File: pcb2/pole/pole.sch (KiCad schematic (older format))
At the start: 21 parts, among them IC1 LMx93, IC2 STM32F0xxKxTx, P1 POWER_IN, P2 BUS_IN, P3 BUS_OUT, P4 SWD_TC, P5 LEDs, Q1 MTM232270LBF, Q2 MTM232270LBF, Q3 MTM232270LBF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

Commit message: Initial layout of f030
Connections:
- net BUS: now also IC2.19 (PA9)
- net NRST: now also C5.2, IC2.4 (NRST)
- net SWDCLK: now also IC2.24 (PA14)
- net SWDIO: now also IC2.23 (PA13)
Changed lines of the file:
@@
 $EndComp
 $Comp
-L GND #PWR5
+L GND #PWR01
 U 1 1 56F1CE8F
 P 3450 3000
-F 0 "#PWR5" H 3450 2750 50  0001 C CNN
+F 0 "#PWR01" H 3450 2750 50  0001 C CNN
 F 1 "GND" H 3450 2850 50  0000 C CNN
 F 2 "" H 3450 3000 50  0000 C CNN
@@
 	3450 2900 3450 3000
 $Comp
-L +12V #PWR4
+L +12V #PWR02
 U 1 1 56F1CF45
 P 3450 2700
-F 0 "#PWR4" H 3450 2550 50  0001 C CNN
+F 0 "#PWR02" H 3450 2550 50  0001 C CNN
 F 1 "+12V" H 3450 2840 50  0000 C CNN
 F 2 "" H 3450 2700 50  0000 C CNN
@@
 	3450 2800 3450 2700
 $Comp
-L PWR_FLAG #FLG1
+L PWR_FLAG #FLG03
 U 1 1 56F1CF7B
 P 3300 2800
-F 0 "#FLG1" H 3300 2895 50  0001 C CNN
+F 0 "#FLG03" H 3300 2895 50  0001 C CNN
 F 1 "PWR_FLAG" H 3300 2980 50  0001 C CNN
 F 2 "" H 3300 2800 50  0000 C CNN
@@
 Connection ~ 3300 2900
 $Comp
-L PWR_FLAG #FLG2
+L PWR_FLAG #FLG04
 U 1 1 56F1CFB0
 P 3300 2900
-F 0 "#FLG2" H 3300 2995 50  0001 C CNN
+F 0 "#FLG04" H 3300 2995 50  0001 C CNN
 F 1 "PWR_FLAG" H 3300 3080 50  0001 C CNN
 F 2 "" H 3300 2900 50  0000 C CNN
@@
 BUS_B
 $Comp
-L GND #PWR3
+L GND #PWR05
 U 1 1 56F1D45F
 P 3150 6050
-F 0 "#PWR3" H 3150 5800 50  0001 C CNN
+F 0 "#PWR05" H 3150 5800 50  0001 C CNN
 F 1 "GND" H 3150 5900 50  0000 C CNN
 F 2 "" H 3150 6050 50  0000 C CNN
@@
 BUS
 $Comp
-L +3V3 #PWR1
+L +3V3 #PWR06
 U 1 1 56F1D52A
 P 3150 5200
-F 0 "#PWR1" H 3150 5050 50  0001 C CNN
+F 0 "#PWR06" H 3150 5050 50  0001 C CNN
 F 1 "+3V3" H 3150 5340 50  0000 C CNN
 F 2 "" H 3150 5200 50  0000 C CNN
@@
 $EndComp
 $Comp
-L GND #PWR2
+L GND #PWR07
 U 1 1 56F1D54C
 P 3150 5400
-F 0 "#PWR2" H 3150 5150 50  0001 C CNN
+F 0 "#PWR07" H 3150 5150 50  0001 C CNN
 F 1 "GND" H 3150 5250 50  0001 C CNN
 F 2 "" H 3150 5400 50  0000 C CNN
@@
 NoConn ~ 7500 2450
 $Comp
-L GND #PWR20
+L GND #PWR08
 U 1 1 56F1D83D
 P 6700 2450
-F 0 "#PWR20" H 6700 2200 50  0001 C CNN
+F 0 "#PWR08" H 6700 2200 50  0001 C CNN
 F 1 "GND" H 6700 2300 50  0000 C CNN
 F 2 "" H 6700 2450 50  0000 C CNN
@@
 $EndComp
 $Comp
-L +3V3 #PWR19
+L +3V3 #PWR09
 U 1 1 56F1D861
 P 6700 2250
-F 0 "#PWR19" H 6700 2100 50  0001 C CNN
+F 0 "#PWR09" H 6700 2100 50  0001 C CNN
 F 1 "+3V3" H 6700 2390 50  0000 C CNN
 F 2 "" H 6700 2250 50  0000 C CNN
@@
 NRST
 $Comp
-L GND #PWR13
+L GND #PWR010
 U 1 1 56F1D8BE
 P 4850 3250
-F 0 "#PWR13" H 4850 3000 50  0001 C CNN
+F 0 "#PWR010" H 4850 3000 50  0001 C CNN
 F 1 "GND" H 4850 3100 50  0000 C CNN
 F 2 "" H 4850 3250 50  0000 C CNN
@@
 $EndComp
 Wire Wire Line
-	4850 3150 4700 3150
-$Comp
-L GND #PWR11
+	4300 3150 4850 3150
+$Comp
+L GND #PWR011
 U 1 1 56F1D93B
 P 4700 3350
-F 0 "#PWR11" H 4700 3100 50  0001 C CNN
+F 0 "#PWR011" H 4700 3100 50  0001 C CNN
 F 1 "GND" H 4700 3200 50  0000 C CNN
 F 2 "" H 4700 3350 50  0000 C CNN
@@
 $EndComp
 $Comp
-L GND #PWR12
+L GND #PWR012
 U 1 1 56F1D985
 P 4850 2950
-F 0 "#PWR12" H 4850 2700 50  0001 C CNN
+F 0 "#PWR012" H 4850 2700 50  0001 C CNN
 F 1 "GND" H 4850 2800 50  0001 C CNN
 F 2 "" H 4850 2950 50  0000 C CNN
@@
 $EndComp
 $Comp
-L +3V3 #PWR7
+L +3V3 #PWR013
 U 1 1 56F1DBBD
 P 4350 2650
-F 0 "#PWR7" H 4350 2500 50  0001 C CNN
+F 0 "#PWR013" H 4350 2500 50  0001 C CNN
 F 1 "+3V3" H 4350 2790 50  0000 C CNN
 F 2 "" H 4350 2650 50  0000 C CNN
@@
 	4500 2850 4350 2850
 $Comp
-L GND #PWR8
+L GND #PWR014
 U 1 1 56F1DC6A
 P 4350 2850
-F 0 "#PWR8" H 4350 2600 50  0001 C CNN
+F 0 "#PWR014" H 4350 2600 50  0001 C CNN
 F 1 "GND" H 4350 2700 50  0000 C CNN
 F 2 "" H 4350 2850 50  0000 C CNN
@@
 	4700 2750 4700 2550
 $Comp
-L +3V3 #PWR9
+L +3V3 #PWR015
 U 1 1 56F1DCD3
 P 4700 2550
-F 0 "#PWR9" H 4700 2400 50  0001 C CNN
+F 0 "#PWR015" H 4700 2400 50  0001 C CNN
 F 1 "+3V3" H 4700 2690 50  0000 C CNN
 F 2 "" H 4700 2550 50  0000 C CNN
@@
 $EndComp
 $Comp
-L GND #PWR10
+L GND #PWR016
 U 1 1 56F1DCFF
 P 4700 2950
-F 0 "#PWR10" H 4700 2700 50  0001 C CNN
+F 0 "#PWR016" H 4700 2700 50  0001 C CNN
 F 1 "GND" H 4700 2800 50  0000 C CNN
 F 2 "" H 4700 2950 50  0000 C CNN
@@
 Connection ~ 4700 2750
 $Comp
-L +12V #PWR26
+L +12V #PWR017
 U 1 1 56F1E092
 P 9600 4000
-F 0 "#PWR26" H 9600 3850 50  0001 C CNN
+F 0 "#PWR017" H 9600 3850 50  0001 C CNN
 F 1 "+12V" H 9600 4140 50  0000 C CNN
 F 2 "" H 9600 4000 50  0000 C CNN
@@
 DRIVE_R
 $Comp
-L GND #PWR21
+L GND #PWR018
 U 1 1 56F1E226
 P 7900 3650
-F 0 "#PWR21" H 7900 3400 50  0001 C CNN
+F 0 "#PWR018" H 7900 3400 50  0001 C CNN
 F 1 "GND" H 7900 3500 50  0000 C CNN
 F 2 "" H 7900 3650 50  0000 C CNN
@@
 DRIVE_G
 $Comp
-L GND #PWR22
+L GND #PWR019
 U 1 1 56F1E522
 P 7900 4400
-F 0 "#PWR22" H 7900 4150 50  0001 C CNN
+F 0 "#PWR019" H 7900 4150 50  0001 C CNN
 F 1 "GND" H 7900 4250 50  0000 C CNN
 F 2 "" H 7900 4400 50  0000 C CNN
@@
 DRIVE_B
 $Comp
-L GND #PWR23
+L GND #PWR020
 U 1 1 56F1E671
 P 7900 5150
-F 0 "#PWR23" H 7900 4900 50  0001 C CNN
+F 0 "#PWR020" H 7900 4900 50  0001 C CNN
 F 1 "GND" H 7900 5000 50  0000 C CNN
 F 2 "" H 7900 5150 50  0000 C CNN
@@
 Text Label 7600 4950 2    60   ~ 0
 LED_B
-Text Label 6150 3050 0    60   ~ 0
+Text Label 5650 3550 0    60   ~ 0
 BUS
 Text Label 6150 3150 0    60   ~ 0
@@
 PIEZO
 $Comp
-L GND #PWR25
+L GND #PWR021
 U 1 1 56F594BA
 P 9550 5800
-F 0 "#PWR25" H 9550 5550 50  0001 C CNN
+F 0 "#PWR021" H 9550 5550 50  0001 C CNN
 F 1 "GND" H 9550 5650 50  0000 C CNN
 F 2 "" H 9550 5800 50  0000 C CNN
@@
 $EndComp
 $Comp
-L +12V #PWR24
+L +12V #PWR022
 U 1 1 56F59754
 P 9550 5200
-F 0 "#PWR24" H 9550 5050 50  0001 C CNN
+F 0 "#PWR022" H 9550 5050 50  0001 C CNN
 F 1 "+12V" H 9550 5340 50  0000 C CNN
 F 2 "" H 9550 5200 50  0000 C CNN
@@
 Connection ~ 4100 5300
 $Comp
-L +3V3 #PWR6
+L +3V3 #PWR023
 U 1 1 56F59A49
 P 4100 5000
-F 0 "#PWR6" H 4100 4850 50  0001 C CNN
+F 0 "#PWR023" H 4100 4850 50  0001 C CNN
 F 1 "+3V3" H 4100 5140 50  0000 C CNN
 F 2 "" H 4100 5000 50  0000 C CNN
@@
 $EndComp
 $Comp
-L +12V #PWR14
+L +12V #PWR024
 U 1 1 56F59EBA
 P 5200 5350
-F 0 "#PWR14" H 5200 5200 50  0001 C CNN
+F 0 "#PWR024" H 5200 5200 50  0001 C CNN
 F 1 "+12V" H 5200 5490 50  0000 C CNN
 F 2 "" H 5200 5350 50  0000 C CNN
@@
 $EndComp
 $Comp
-L GND #PWR15
+L GND #PWR025
 U 1 1 56F59F39
 P 5200 5650
-F 0 "#PWR15" H 5200 5400 50  0001 C CNN
+F 0 "#PWR025" H 5200 5400 50  0001 C CNN
 F 1 "GND" H 5200 5500 50  0000 C CNN
 F 2 "" H 5200 5650 50  0000 C CNN
@@
 	5200 5350 5300 5350
 $Comp
-L +3V3 #PWR17
+L +3V3 #PWR026
 U 1 1 56F59FB2
 P 6200 5350
-F 0 "#PWR17" H 6200 5200 50  0001 C CNN
+F 0 "#PWR026" H 6200 5200 50  0001 C CNN
 F 1 "+3V3" H 6200 5490 50  0000 C CNN
 F 2 "" H 6200 5350 50  0000 C CNN
@@
 $EndComp
 $Comp
-L GND #PWR18
+L GND #PWR027
 U 1 1 56F5A070
 P 6200 5650
-F 0 "#PWR18" H 6200 5400 50  0001 C CNN
+F 0 "#PWR027" H 6200 5400 50  0001 C CNN
 F 1 "GND" H 6200 5500 50  0000 C CNN
 F 2 "" H 6200 5650 50  0000 C CNN
@@
 $EndComp
 $Comp
-L GND #PWR16
+L GND #PWR028
 U 1 1 56F5A0AE
 P 5700 5650
-F 0 "#PWR16" H 5700 5400 50  0001 C CNN
+F 0 "#PWR028" H 5700 5400 50  0001 C CNN
 F 1 "GND" H 5700 5500 50  0000 C CNN
 F 2 "" H 5700 5650 50  0000 C CNN
@@
 	1    0    0    -1
 $EndComp
+Text Label 4300 3150 2    60   ~ 0
+NRST
+Text Label 5650 3950 0    60   ~ 0
+SWDIO
+Text Label 5650 4050 0    60   ~ 0
+SWDCLK
+Connection ~ 4700 3150
 $EndSCHEMATC

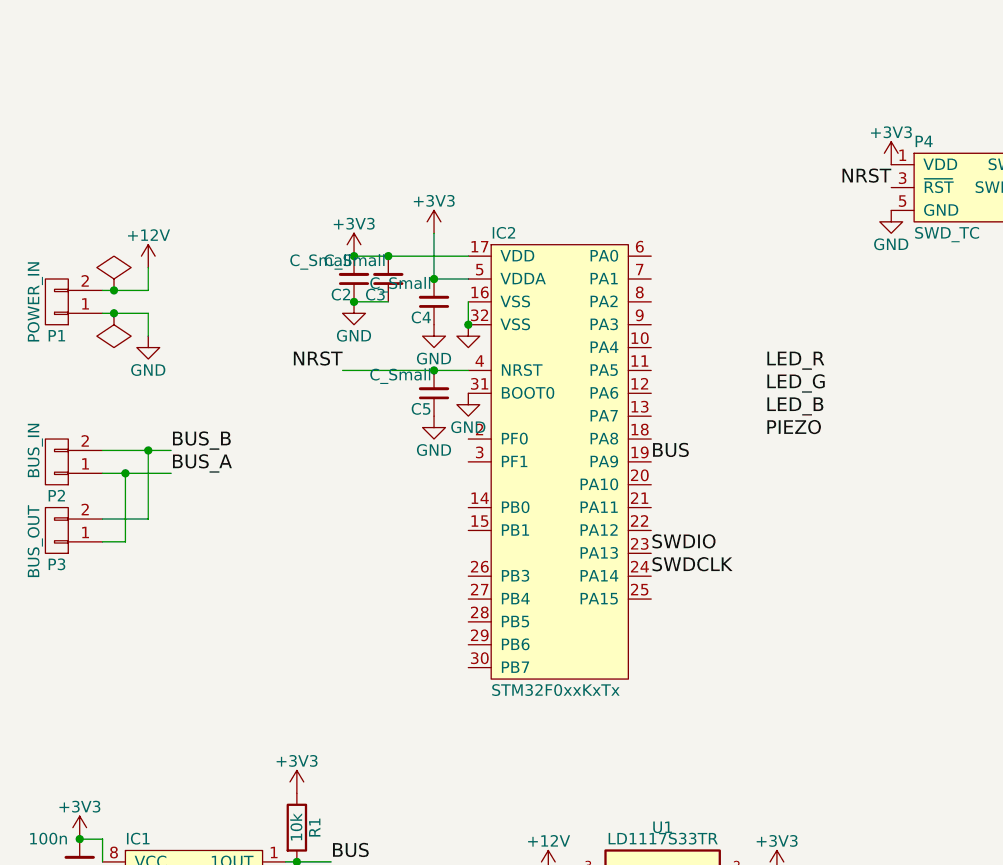
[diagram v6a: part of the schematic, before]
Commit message: Use STM32F051, changed FPs to agg-kicad
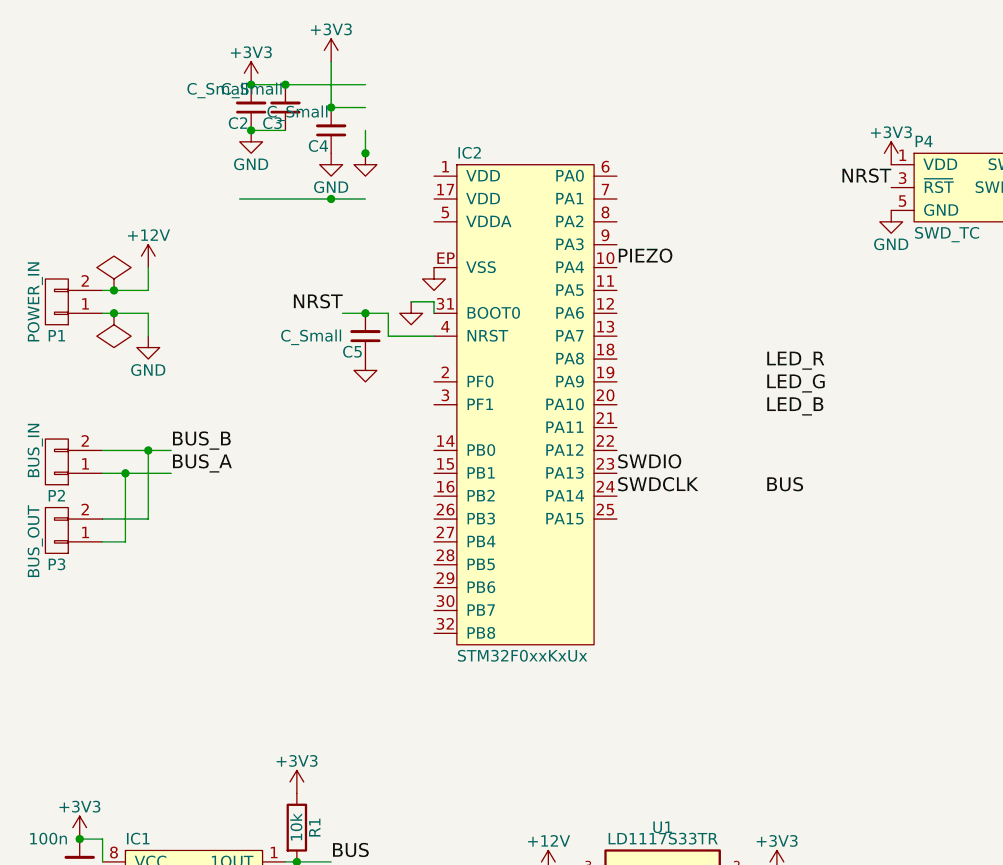
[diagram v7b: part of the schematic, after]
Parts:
- removed IC2: STM32F0xxKxTx, agg:LQFP-32, symbol STM32F0xxKxTx
- added IC2: STM32F0xxKxUx, agg:QFN-32-EP-ST, symbol STM32F0xxKxUx
- Q1, Q2, Q3, Q4: footprint thegrid:SOT-323 -> agg:SOT-323
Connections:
- wire segments 25 -> 30
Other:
- moved on the sheet: C2, C3, C4, C5

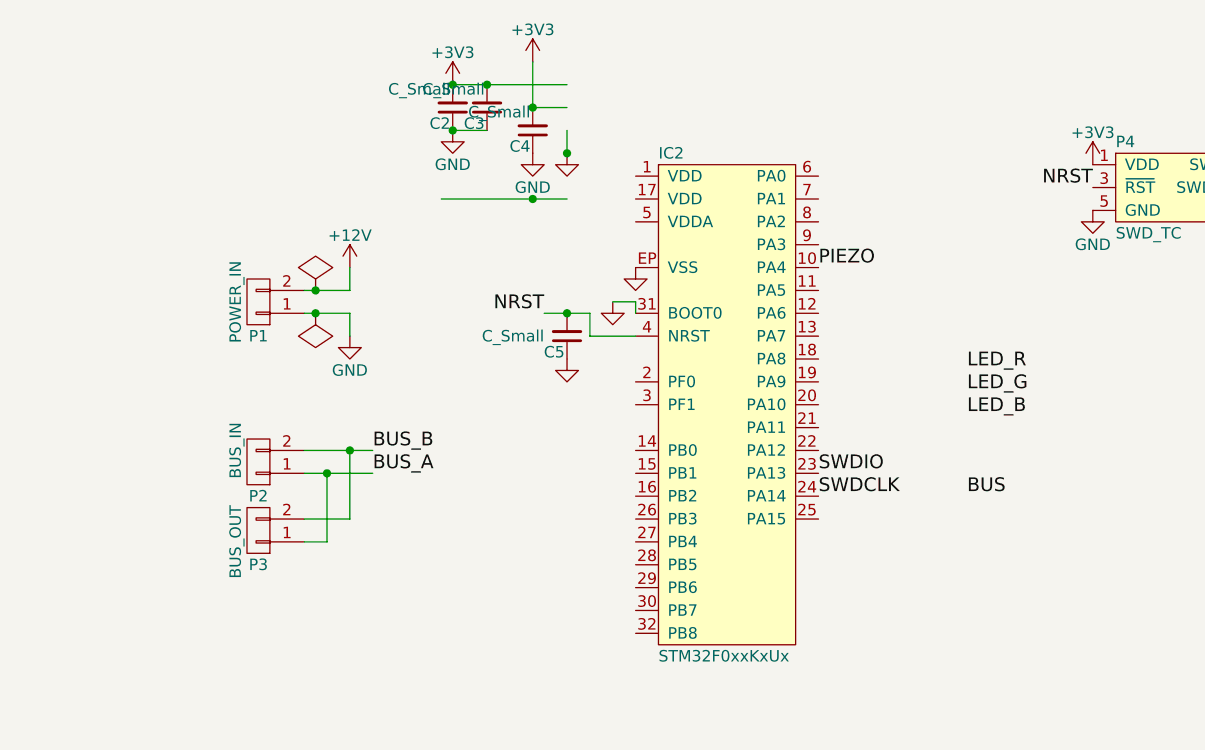
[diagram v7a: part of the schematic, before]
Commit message: Finished pin assignments, first layout
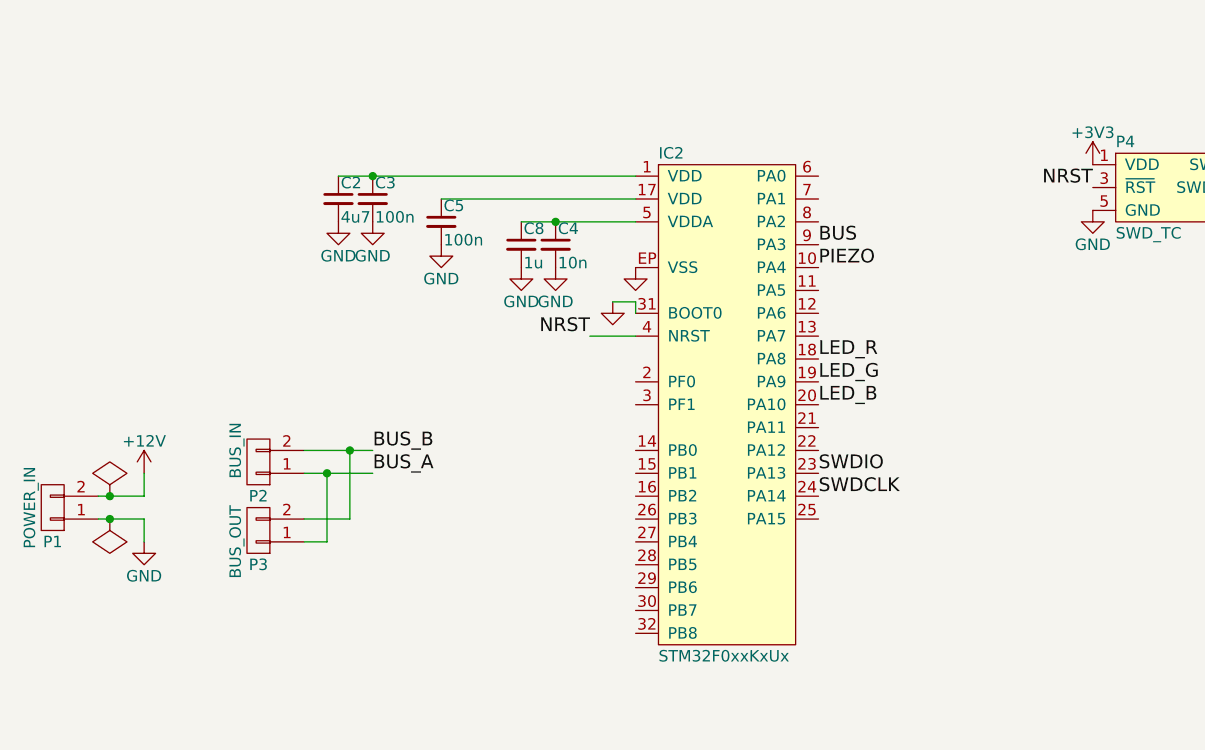
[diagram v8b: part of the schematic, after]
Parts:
- added C8: 1u, agg:0603, symbol C_Small
- C2: value C_Small -> 4u7
- C3, C5: value C_Small -> 100n
- C4: value C_Small -> 10n
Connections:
- wire segments 30 -> 25
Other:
- moved on the sheet: C2, C3, C4, P1
